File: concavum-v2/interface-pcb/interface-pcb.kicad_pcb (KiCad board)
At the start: 2 copper layers, 36 x 42 mm, 8 parts, among them J1 Audio_Jack, J2 FPC_connector, U1 Adafruit_KB2040

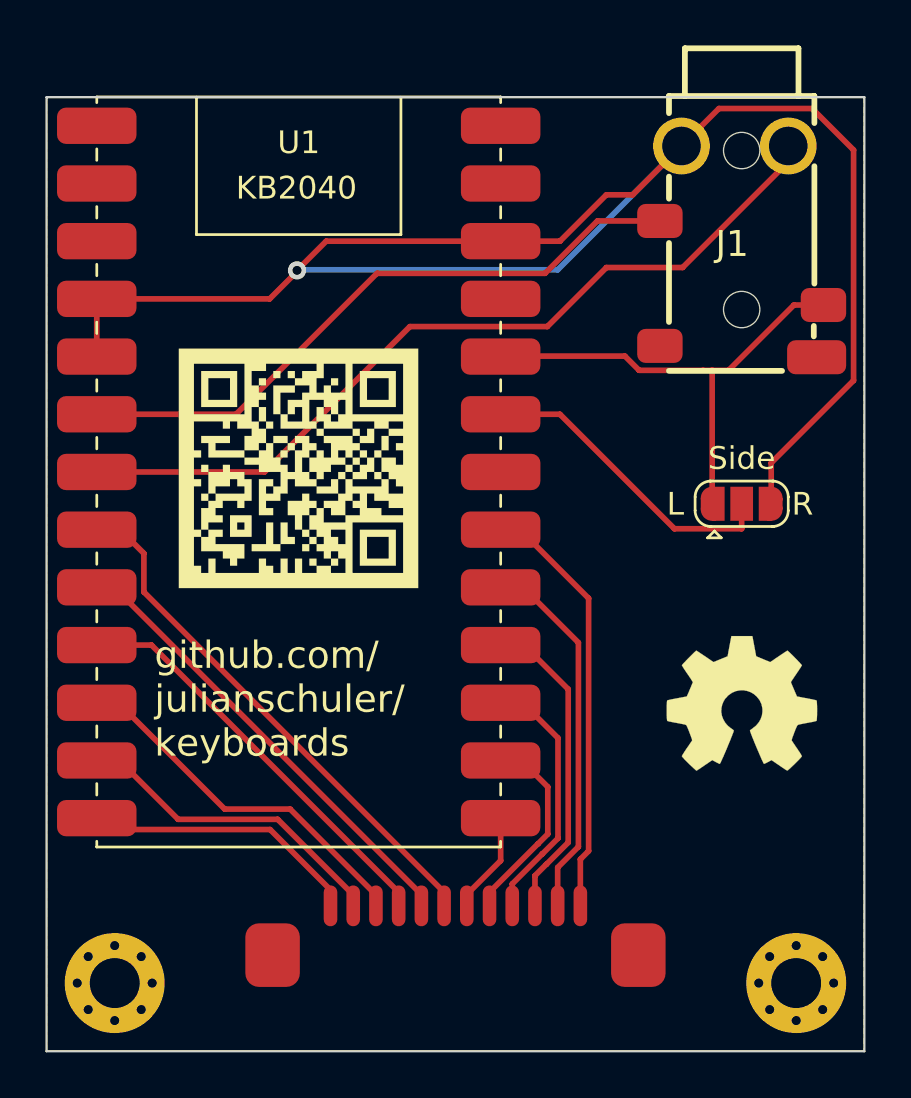
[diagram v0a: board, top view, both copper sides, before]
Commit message: Implement VBUS detection and make PCB symmetric
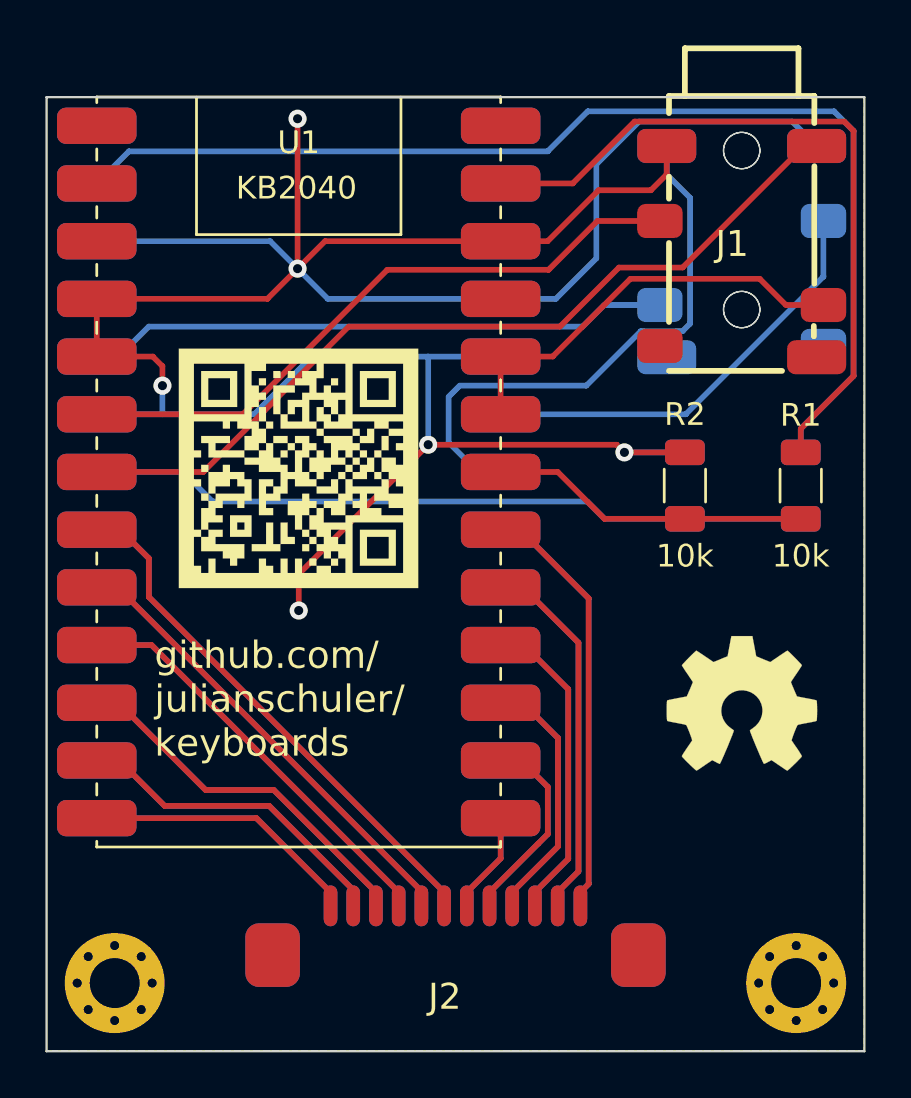
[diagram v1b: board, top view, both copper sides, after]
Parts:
- removed JP1: Side, Jumper:SolderJumper-3_P1.3mm_Open_RoundedPad1.0x1.5mm
- removed the REF** at (159.1, 96.7)
- added J3: Audio_Jack, Custom:Audio_Jack, B.Cu at (163.6, 82.8)
- added J4: FFC_connector, Custom:FPC_Connector, B.Cu at (151.0, 111.6)
- added R1: 10k, Resistor_SMD:R_1206_3216Metric, F.Cu at (166.2, 93.1)
- added R2: 10k, Resistor_SMD:R_1206_3216Metric, F.Cu at (161.1, 93.1)
- added R3: 10k, Resistor_SMD:R_1206_3216Metric, B.Cu at (166.2, 93.1)
- added R4: 10k, Resistor_SMD:R_1206_3216Metric, B.Cu at (161.1, 93.1)
- added REF**: OSHW-Symbol_6.7x6mm_SilkScreen, Symbol:OSHW-Symbol_6.7x6mm_SilkScreen, B.Cu at (163.6, 102.7)
- added U2: Adafruit_KB2040, Custom:Adafruit_KB2040, B.Cu at (144.1, 92.5)
- J2: value FPC_connector -> FFC_connector
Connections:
- net /COL1 renamed /L_COL1
- net /COL2 renamed /L_COL2
- net /COL3 renamed /L_COL3
- net /COL4 renamed /L_COL4
- net /COL5 renamed /L_COL5
- net /COL6 renamed /L_COL6
- net /ROW1 renamed /L_ROW1
- net /ROW2 renamed /L_ROW2
- net /ROW3 renamed /L_ROW3
- net /ROW4 renamed /L_ROW4
- net /ROW5 renamed /L_ROW5
- net /ROW6 renamed /L_ROW6
- net /SCL renamed /L_RX
- net /SDA renamed /L_TX
- J1 pad T: +3V3 -> +3V3_L
- U1 pad 20: unconnected-(U1-A2-Pad20) -> Net-(U1-A2)
- U1 pad 21: Net-(JP1-C) -> +3V3_L
- U1 pad 22: +3V3 -> +3V3_L
- U1 pad 25: unconnected-(U1-RAW-Pad25) -> Net-(U1-RAW)
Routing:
- net GND: track 76.4 -> 128.3 mm, vias 1 -> 6
- net Net-(U2-RAW): track 0.00 -> 50.1 mm
- net Net-(U1-RAW): track 0.00 -> 32.0 mm
- net Net-(U2-A2): track 0.00 -> 31.8 mm
- net +3V3_R: track 0.00 -> 25.7 mm
- net /R_RX: track 0.00 -> 25.0 mm
- net /R_COL2: track 0.00 -> 23.5 mm
- net +3V3: track 22.5 -> 0.00 mm
- net /R_COL3: track 0.00 -> 20.5 mm
- net /R_TX: track 0.00 -> 19.2 mm
- net /R_COL1: track 0.00 -> 18.8 mm
- net +3V3_L: track 0.00 -> 18.6 mm
- net /R_COL4: track 0.00 -> 18.4 mm
- net /R_ROW6: track 0.00 -> 16.4 mm
- net /R_COL5: track 0.00 -> 16.3 mm
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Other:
- board text added: "Adafruit_KB2040"
- board text added: "KB2040"
- board text added: "U1"
- board text removed: "Concavum v2"
- board text removed: "L"
- board text removed: "R"
- board text removed: "github.com/julianschuler/keyboards"

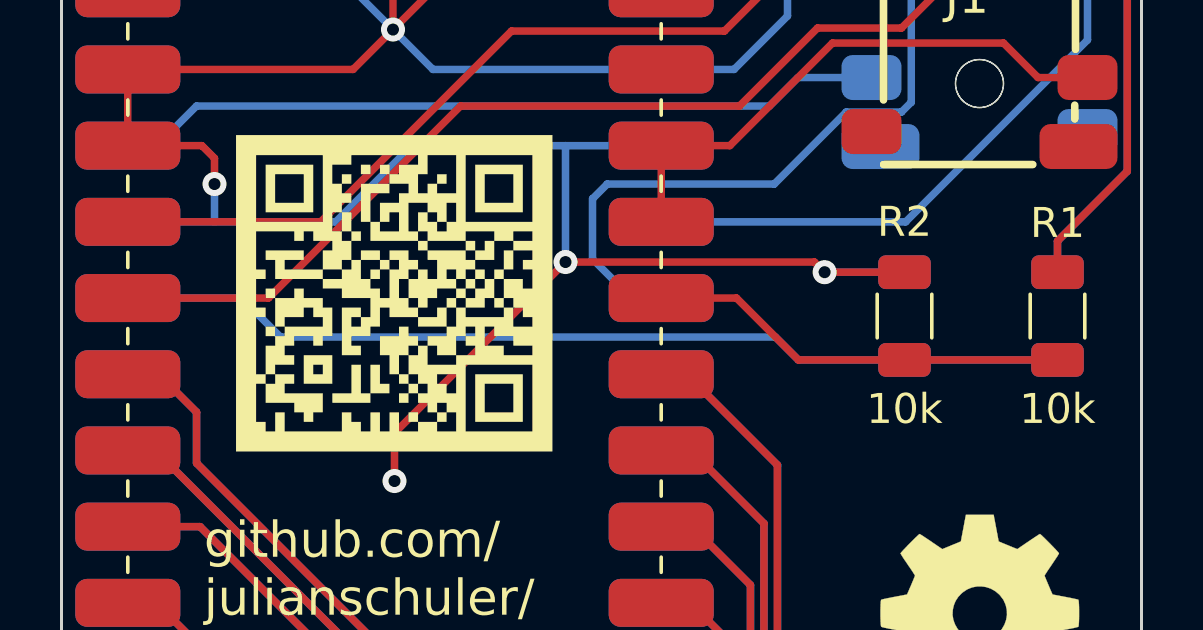
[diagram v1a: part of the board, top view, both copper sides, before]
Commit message: Use a zener diode for VBUS detection circuit
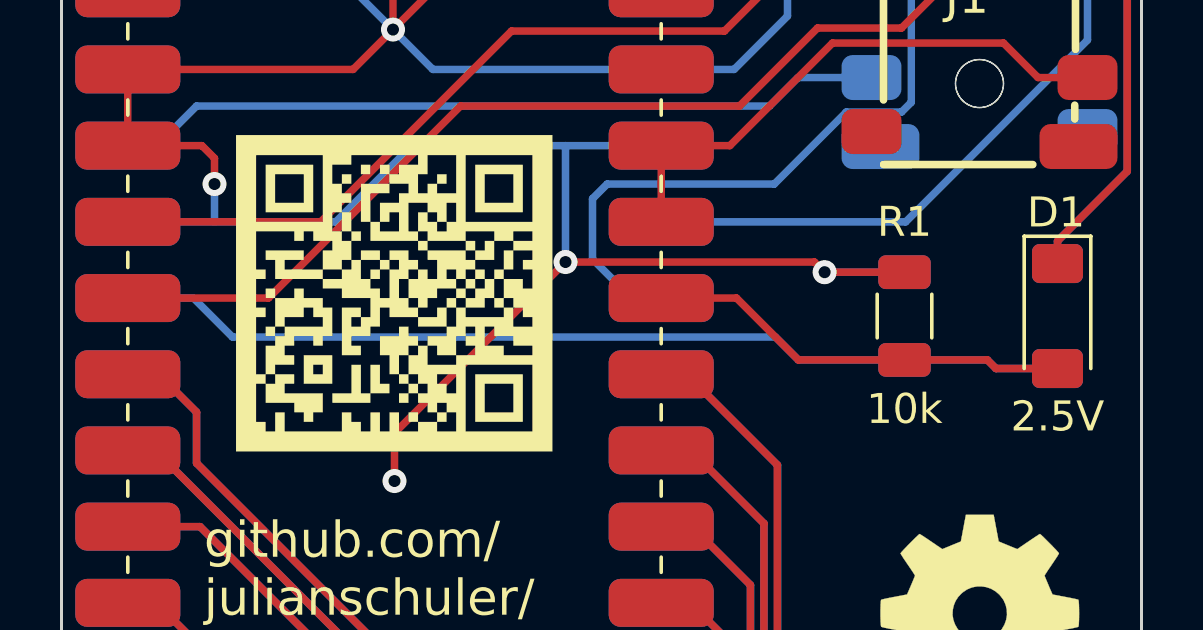
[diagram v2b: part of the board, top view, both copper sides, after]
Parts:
- removed the R1 at (166.2, 93.1)
- removed R3: 10k, Resistor_SMD:R_1206_3216Metric
- added D1: 2.5V, Diode_SMD:D_MiniMELF, F.Cu at (166.2, 93.1)
- added D2: 2.5V, Diode_SMD:D_MiniMELF, B.Cu at (166.2, 93.1)
- renumbered R2 to R1, R4 to R2

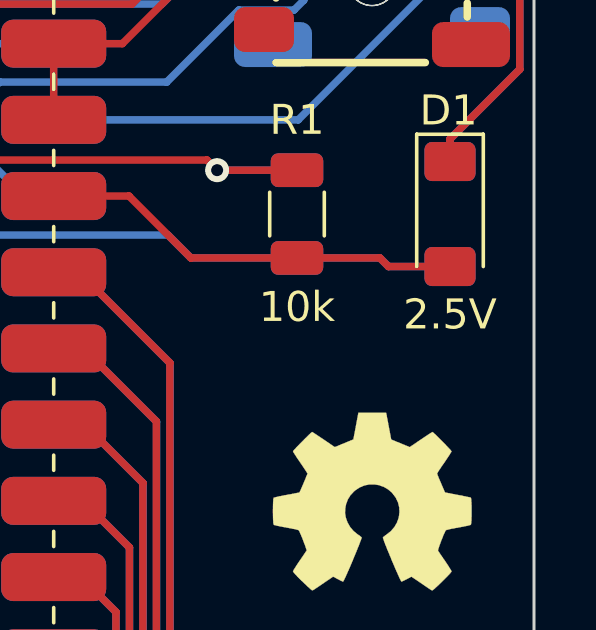
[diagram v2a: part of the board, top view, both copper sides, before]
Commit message: Replace 2.5V zener diode with 3.6V one
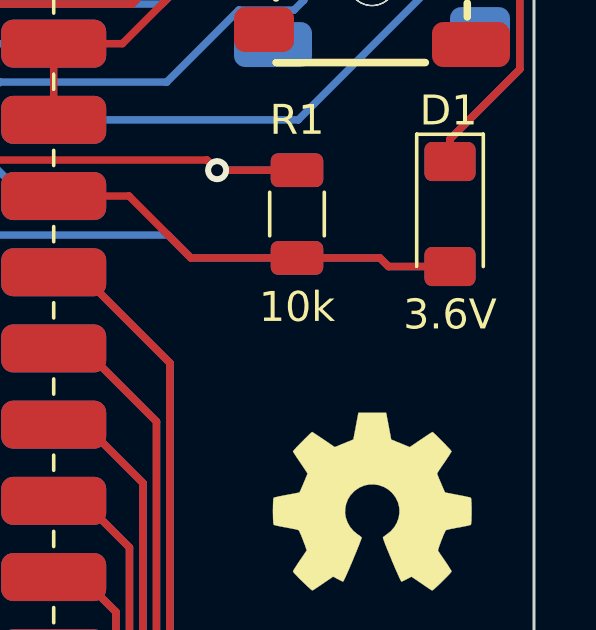
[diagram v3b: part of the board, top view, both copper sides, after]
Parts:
- D1, D2: value 2.5V -> 3.6V
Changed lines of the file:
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@@
 			)
 		)
-		(property "Value" "2.5V"
+		(property "Value" "3.6V"
 			(at 3.35 0 180)
 			(layer "F.SilkS")
@@
 			)
 		)
-		(property "Value" "2.5V"
+		(property "Value" "3.6V"
 			(at 3.4 0 0)
 			(layer "B.SilkS")
